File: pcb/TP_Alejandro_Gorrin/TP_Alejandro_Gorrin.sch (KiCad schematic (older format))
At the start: 32 parts, among them J1 Conn_01x12, J2 Conn_01x02, J3 Conn_01x16, J4 USB_B_Micro, Q1 MMBT3904, Q2 MMBT3904, Q3 BS250, SW1 SW_1, U1 MCP73831-2-OT, U3 CP2104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

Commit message: PCB conexiones realizadas
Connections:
- net +3V3: now also J3.1 (Pin_1); no longer J3.15 (Pin_15)
- net A0_DAC2: now also J1.6 (Pin_6); no longer J3.12 (Pin_12)
- net A1_DAC1: now also J1.7 (Pin_7); no longer J3.11 (Pin_11)
- net A2_I34: now also J1.10 (Pin_10); no longer J3.10 (Pin_10)
- net A3_I39: now also J1.11 (Pin_11); no longer J3.9 (Pin_9)
- net A4_IO36: now also J1.12 (Pin_12); no longer J3.8 (Pin_8)
- net A5_IO4: now also J3.8 (Pin_8); no longer J3.7 (Pin_7)
- net EN: now also J3.4 (Pin_4); no longer J1.2 (Pin_2)
- net GNDD: now also J3.3 (Pin_3); no longer J3.13 (Pin_13)
- net IO12_A11: now also J1.3 (Pin_3); no longer J1.5 (Pin_5)
- net IO13_A12: now also J3.6 (Pin_6); no longer J1.4 (Pin_4)
- net IO14_A6: now also J1.4 (Pin_4); no longer J1.10 (Pin_10)
- net IO15_A8: now also J3.7 (Pin_7); no longer J1.8 (Pin_8)
- net IO16: now also J3.9 (Pin_9); no longer J3.3 (Pin_3)
- net IO17: now also J3.10 (Pin_10); no longer J3.2 (Pin_2)
- net IO21: now also J3.14 (Pin_14); no longer J3.1 (Pin_1)
- net IO27_A10: now also J1.5 (Pin_5); no longer J1.6 (Pin_6)
- net IO33_A9: now also J1.8 (Pin_8); no longer J1.7 (Pin_7)
- net MISI: now also J3.12 (Pin_12); no longer J3.5 (Pin_5)
- net MISO: now also J3.13 (Pin_13); no longer J3.4 (Pin_4)
- net RESET: now also J3.2 (Pin_2); no longer J3.16 (Pin_16)
- net SCI: now also J3.15 (Pin_15); no longer J1.11 (Pin_11)
- net SCK: now also J3.11 (Pin_11); no longer J3.6 (Pin_6)
- net SDA: now also J3.16 (Pin_16); no longer J1.12 (Pin_12)
- net VBUS: now also J1.2 (Pin_2); no longer J1.3 (Pin_3)
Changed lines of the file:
@@
 Wire Wire Line
 	3775 6225 3775 6375
-Wire Wire Line
-	3775 5925 3775 5850
 $Comp
 L Transistor_FET:BS250 Q3
@@
 Wire Wire Line
 	6250 4800 5900 4800
-Text Label 5900 4800 0    45   ~ 0
+Text Label 7400 4700 0    45   ~ 0
 IO13_A12
 Text Label 1750 5275 1    47   ~ 0
@@
 $EndComp
 Wire Wire Line
-	6250 4700 5700 4700
-Wire Wire Line
-	5700 4700 5700 4600
+	5700 4600 5700 4500
 Wire Wire Line
 	6250 4500 5900 4500
@@
 L power:VBUS #PWR0122
 U 1 1 5F8AB477
-P 5700 4600
-F 0 "#PWR0122" H 5700 4450 50  0001 C CNN
-F 1 "VBUS" H 5715 4773 50  0000 C CNN
-F 2 "" H 5700 4600 50  0001 C CNN
-F 3 "" H 5700 4600 50  0001 C CNN
-	1    5700 4600
+P 5700 4500
+F 0 "#PWR0122" H 5700 4350 50  0001 C CNN
+F 1 "VBUS" H 5700 4650 50  0000 C CNN
+F 2 "" H 5700 4500 50  0001 C CNN
+F 3 "" H 5700 4500 50  0001 C CNN
+	1    5700 4500
 	1    0    0    -1
 $EndComp
@@
 	1    0    0    -1
 $EndComp
-Wire Wire Line
-	7700 5400 7000 5400
-Wire Wire Line
-	7000 5400 7000 5500
 $Comp
 L power:GNDD #PWR0129
 U 1 1 5F8BAE19
-P 7000 5500
-F 0 "#PWR0129" H 7000 5250 50  0001 C CNN
-F 1 "GNDD" H 7004 5345 50  0000 C CNN
-F 2 "" H 7000 5500 50  0001 C CNN
-F 3 "" H 7000 5500 50  0001 C CNN
-	1    7000 5500
-	1    0    0    -1
-$EndComp
-Wire Wire Line
-	7700 5600 7350 5600
-Wire Wire Line
-	7350 5600 7350 5550
+P 7125 4500
+F 0 "#PWR0129" H 7125 4250 50  0001 C CNN
+F 1 "GNDD" H 7129 4345 50  0000 C CNN
+F 2 "" H 7125 4500 50  0001 C CNN
+F 3 "" H 7125 4500 50  0001 C CNN
+	1    7125 4500
+	1    0    0    -1
+$EndComp
 $Comp
 L power:+3.3V #PWR0130
 U 1 1 5F8BF3BE
-P 7350 5550
-F 0 "#PWR0130" H 7350 5400 50  0001 C CNN
-F 1 "+3.3V" H 7500 5600 50  0000 C CNN
-F 2 "" H 7350 5550 50  0001 C CNN
-F 3 "" H 7350 5550 50  0001 C CNN
-	1    7350 5550
+P 7300 4150
+F 0 "#PWR0130" H 7300 4000 50  0001 C CNN
+F 1 "+3.3V" H 7450 4200 50  0000 C CNN
+F 2 "" H 7300 4150 50  0001 C CNN
+F 3 "" H 7300 4150 50  0001 C CNN
+	1    7300 4150
 	1    0    0    -1
 $EndComp
@@
 	6250 5600 5900 5600
 Wire Wire Line
-	7700 4200 7400 4200
-Wire Wire Line
 	7700 4300 7400 4300
 Wire Wire Line
-	7700 4400 7400 4400
-Wire Wire Line
 	7700 4500 7400 4500
-Wire Wire Line
-	7700 4600 7400 4600
 Wire Wire Line
 	7700 4700 7400 4700
@@
 Text Label 775  3575 0    47   ~ 0
 A3_I39
-Text Label 7400 4900 0    47   ~ 0
+Text Label 5900 5600 0    47   ~ 0
 A4_IO36
-Text Label 7400 5000 0    47   ~ 0
+Text Label 5900 5500 0    47   ~ 0
 A3_I39
 Text Label 3150 3925 0    47   ~ 0
 SCK
-Text Label 7400 4700 0    47   ~ 0
+Text Label 7400 5200 0    47   ~ 0
 SCK
-Wire Wire Line
-	6250 4600 5900 4600
-Text Label 5900 4900 0    47   ~ 0
+Text Label 5900 4700 0    47   ~ 0
 IO12_A11
 Text Label 775  4475 0    47   ~ 0
 IO12_A11
-Text Label 5900 5000 0    47   ~ 0
+Text Label 5900 4900 0    47   ~ 0
 IO27_A10
 Text Label 775  4275 0    47   ~ 0
 IO27_A10
-Text Label 5900 5100 0    47   ~ 0
+Text Label 5900 5200 0    47   ~ 0
 IO33_A9
 Text Label 775  3975 0    47   ~ 0
 IO33_A9
-Text Label 5900 5200 0    47   ~ 0
+Text Label 7400 4800 0    47   ~ 0
 IO15_A8
 Text Label 2450 5275 1    47   ~ 0
@@
 Text Label 775  3875 0    47   ~ 0
 IO32_A7
-Text Label 5900 5400 0    47   ~ 0
+Text Label 5900 4800 0    47   ~ 0
 IO14_A6
 Text Label 775  4375 0    47   ~ 0
 IO14_A6
-Text Label 5900 5500 0    47   ~ 0
+Text Label 7400 5600 0    47   ~ 0
 SCI
 Text Label 3150 3225 0    47   ~ 0
@@
 Text Label 3150 3125 0    47   ~ 0
 SDA
-Text Label 5900 5600 0    47   ~ 0
+Text Label 7400 5700 0    47   ~ 0
 SDA
-Text Label 7400 4200 0    47   ~ 0
+Text Label 7400 5500 0    47   ~ 0
 IO21
 Text Label 3150 3525 0    47   ~ 0
 IO21
-Text Label 7400 4300 0    47   ~ 0
+Text Label 7400 5100 0    47   ~ 0
 IO17
-Text Label 7400 4400 0    47   ~ 0
+Text Label 7400 5000 0    47   ~ 0
 IO16
 Text Label 3150 4025 0    47   ~ 0
@@
 Text Label 3150 4125 0    47   ~ 0
 IO16
-Text Label 7400 4500 0    47   ~ 0
+Text Label 7400 5400 0    47   ~ 0
 MISO
 Text Label 3150 3725 0    47   ~ 0
 MISO
-Text Label 7400 4600 0    47   ~ 0
+Text Label 7400 5300 0    47   ~ 0
 MISI
 Text Label 3150 3825 0    47   ~ 0
 MISI
-Text Label 7400 4800 0    47   ~ 0
+Text Label 7400 4900 0    47   ~ 0
 A5_IO4
 Text Label 3150 4225 0    47   ~ 0
 A5_IO4
-Text Label 7400 5100 0    47   ~ 0
+Text Label 5900 5400 0    47   ~ 0
 A2_I34
 Text Label 775  3675 0    47   ~ 0
 A2_I34
-Text Label 7400 5200 0    47   ~ 0
+Text Label 5900 5100 0    47   ~ 0
 A1_DAC1
 Text Label 775  4075 0    47   ~ 0
 A1_DAC1
-Text Label 7400 5300 0    47   ~ 0
+Text Label 5900 5000 0    47   ~ 0
 A0_DAC2
 Text Label 775  4175 0    47   ~ 0
 A0_DAC2
-Text Label 7400 5700 0    47   ~ 0
+Text Label 7400 4300 0    47   ~ 0
 RESET
 Text Label 4475 3100 0    47   ~ 0
@@
 Text Notes 2225 725  0    55   ~ 11
 POWER_AND_FILTERING
-Text Label 5900 4600 0    47   ~ 0
+Text Label 7400 4500 0    47   ~ 0
 EN
 NoConn ~ 7675 1050
@@
 NoConn ~ 6775 2250
 NoConn ~ 6775 2150
-NoConn ~ 7700 5500
 $Comp
 L Switch:SW_DPST_x2 SW1
@@
 	1875 1325 1750 1325
 Connection ~ 1625 1325
-NoConn ~ 6250 4600
+NoConn ~ 7700 4600
 Wire Wire Line
 	725  725  725  1025
@@
 Wire Wire Line
 	6150 2250 6325 2250
-Wire Wire Line
-	6325 1550 6325 1875
 Wire Wire Line
 	6425 2550 6150 2550
@@
 	1    0    0    -1
 $EndComp
-$Comp
-L power:PWR_FLAG #FLG0103
-U 1 1 5F8B58E7
-P 6225 1875
-F 0 "#FLG0103" H 6225 1950 50  0001 C CNN
-F 1 "PWR_FLAG" V 6225 2025 50  0000 L CNN
-F 2 "" H 6225 1875 50  0001 C CNN
-F 3 "~" H 6225 1875 50  0001 C CNN
-	1    6225 1875
-	0    -1   -1   0
-$EndComp
-Wire Wire Line
-	6225 1875 6325 1875
-Connection ~ 6325 1875
-Wire Wire Line
-	6325 1875 6325 2250
-$Comp
-L power:PWR_FLAG #FLG0105
-U 1 1 5F8C7B1A
-P 3850 5850
-F 0 "#FLG0105" H 3850 5925 50  0001 C CNN
-F 1 "PWR_FLAG" V 3950 5900 50  0000 L CNN
-F 2 "" H 3850 5850 50  0001 C CNN
-F 3 "~" H 3850 5850 50  0001 C CNN
-	1    3850 5850
-	0    1    1    0
-$EndComp
-Wire Wire Line
-	3850 5850 3775 5850
-Connection ~ 3775 5850
-Wire Wire Line
-	3775 5850 3775 5775
 Wire Wire Line
 	3225 1675 3225 2000
@@
 NoConn ~ 2550 4925
 Wire Wire Line
-	5850 2850 5850 3000
-Wire Wire Line
 	4400 1925 4400 1950
 Wire Wire Line
@@
 $EndComp
 NoConn ~ 6150 2650
+Wire Wire Line
+	5700 4600 6250 4600
+Wire Wire Line
+	6250 4700 5900 4700
+Wire Wire Line
+	7300 4200 7300 4150
+Wire Wire Line
+	7300 4200 7700 4200
+Wire Wire Line
+	7700 5400 7400 5400
+Wire Wire Line
+	7700 5500 7400 5500
+Wire Wire Line
+	7700 5600 7400 5600
+Wire Wire Line
+	7125 4400 7125 4500
+Wire Wire Line
+	7125 4400 7700 4400
+NoConn ~ 7700 4500
+Wire Wire Line
+	3775 5775 3775 5925
+Wire Wire Line
+	5850 2850 5850 3000
+Wire Wire Line
+	6325 1550 6325 2250
 $EndSCHEMATC

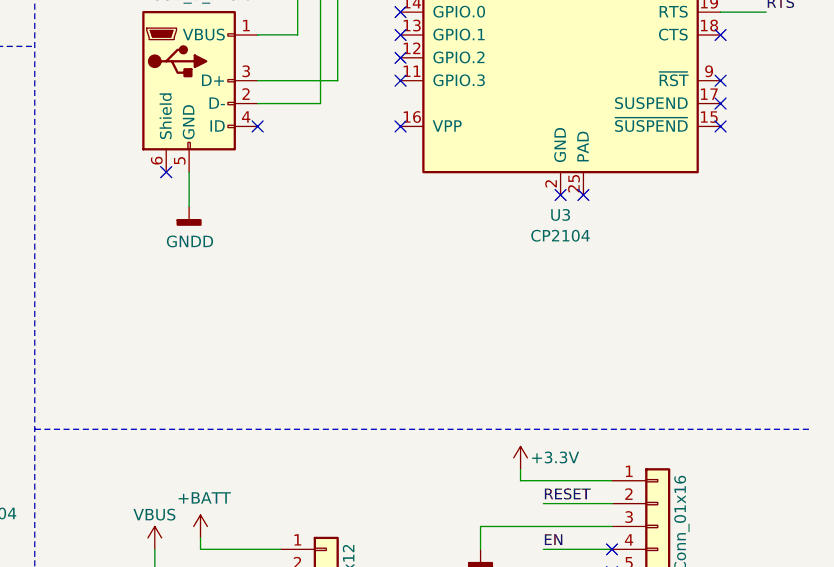
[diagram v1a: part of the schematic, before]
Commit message: Cambio y agrego vias para facilitar el ruteo
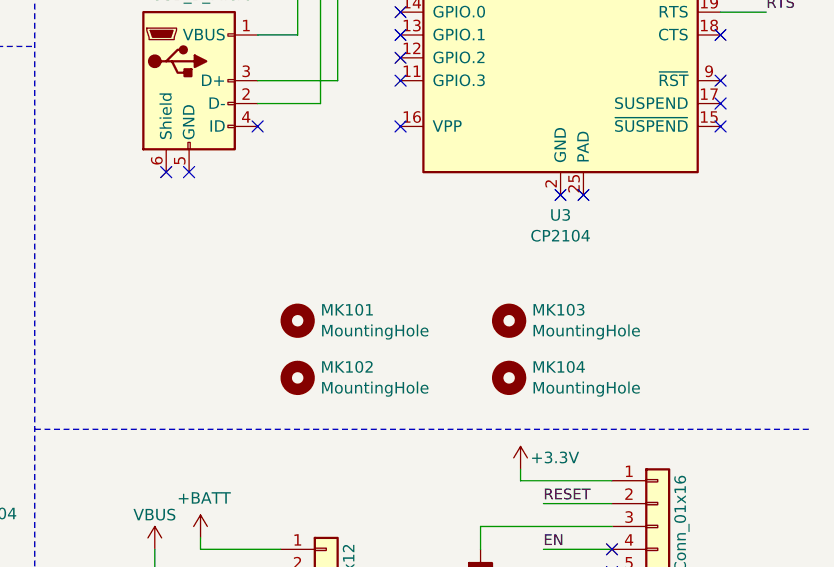
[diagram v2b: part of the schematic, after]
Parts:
- added MK101, MK102, MK103, MK104: MountingHole, MountingHole:MountingHole_2.2mm_M2_DIN965_Pad, symbol Mechanical:MountingHole
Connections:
- net GNDD: no longer J4.5 (GND)
- no-connect marks 28 -> 29
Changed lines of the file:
@@
 Wire Wire Line
 	5925 1200 5925 1250
-$Comp
-L power:GNDD #PWR0112
-U 1 1 5F8A1CC4
-P 5850 3000
-F 0 "#PWR0112" H 5850 2750 50  0001 C CNN
-F 1 "GNDD" H 5854 2845 50  0000 C CNN
-F 2 "" H 5850 3000 50  0001 C CNN
-F 3 "" H 5850 3000 50  0001 C CNN
-	1    5850 3000
-	1    0    0    -1
-$EndComp
 Wire Wire Line
 	5925 1200 6525 1200
@@
 	3775 5775 3775 5925
 Wire Wire Line
-	5850 2850 5850 3000
-Wire Wire Line
 	6325 1550 6325 2250
+NoConn ~ 5850 2850
+$Comp
+L Mechanical:MountingHole MK101
+U 1 1 5FB548C1
+P 6325 3500
+F 0 "MK101" H 6425 3546 50  0000 L CNN
+F 1 "MountingHole" H 6425 3455 50  0000 L CNN
+F 2 "MountingHole:MountingHole_2.2mm_M2_DIN965_Pad" H 6325 3500 50  0001 C CNN
+F 3 "~" H 6325 3500 50  0001 C CNN
+	1    6325 3500
+	1    0    0    -1
+$EndComp
+$Comp
+L Mechanical:MountingHole MK102
+U 1 1 5FB54F64
+P 6325 3750
+F 0 "MK102" H 6425 3796 50  0000 L CNN
+F 1 "MountingHole" H 6425 3705 50  0000 L CNN
+F 2 "MountingHole:MountingHole_2.2mm_M2_DIN965_Pad" H 6325 3750 50  0001 C CNN
+F 3 "~" H 6325 3750 50  0001 C CNN
+	1    6325 3750
+	1    0    0    -1
+$EndComp
+$Comp
+L Mechanical:MountingHole MK103
+U 1 1 5FB55716
+P 7250 3500
+F 0 "MK103" H 7350 3546 50  0000 L CNN
+F 1 "MountingHole" H 7350 3455 50  0000 L CNN
+F 2 "MountingHole:MountingHole_2.2mm_M2_DIN965_Pad" H 7250 3500 50  0001 C CNN
+F 3 "~" H 7250 3500 50  0001 C CNN
+	1    7250 3500
+	1    0    0    -1
+$EndComp
+$Comp
+L Mechanical:MountingHole MK104
+U 1 1 5FB5612A
+P 7250 3750
+F 0 "MK104" H 7350 3796 50  0000 L CNN
+F 1 "MountingHole" H 7350 3705 50  0000 L CNN
+F 2 "MountingHole:MountingHole_2.2mm_M2_DIN965_Pad" H 7250 3750 50  0001 C CNN
+F 3 "~" H 7250 3750 50  0001 C CNN
+	1    7250 3750
+	1    0    0    -1
+$EndComp
 $EndSCHEMATC

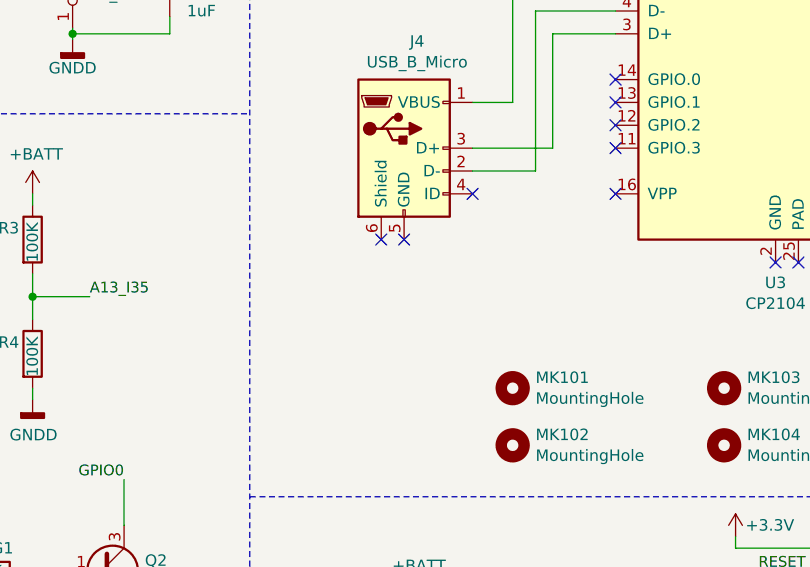
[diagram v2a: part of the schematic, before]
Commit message: Se observa problema con GNDD
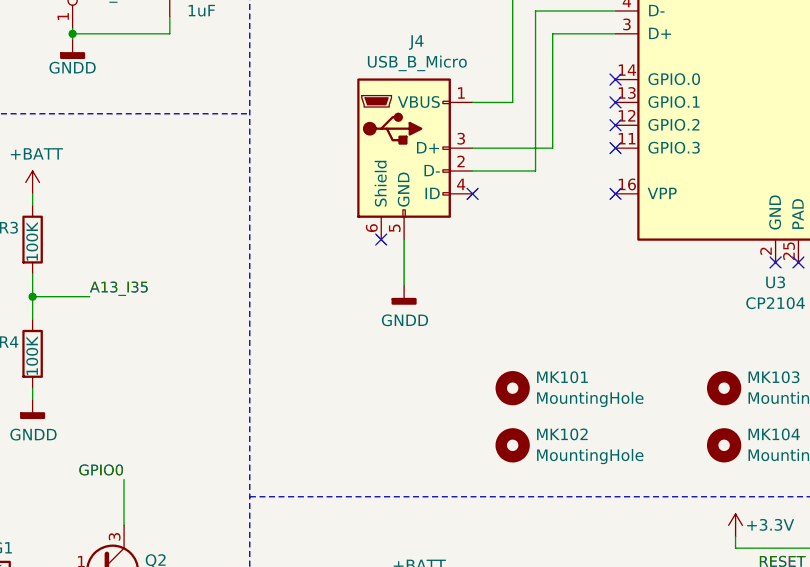
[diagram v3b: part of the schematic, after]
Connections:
- net GNDD: now also J4.5 (GND)
- no-connect marks 29 -> 28
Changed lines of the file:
@@
 Wire Wire Line
 	6325 1550 6325 2250
-NoConn ~ 5850 2850
 $Comp
 L Mechanical:MountingHole MK101
@@
 	1    0    0    -1
 $EndComp
+$Comp
+L power:GNDD #PWR?
+U 1 1 5FB6B73A
+P 5850 3050
+F 0 "#PWR?" H 5850 2800 50  0001 C CNN
+F 1 "GNDD" H 5854 2895 50  0000 C CNN
+F 2 "" H 5850 3050 50  0001 C CNN
+F 3 "" H 5850 3050 50  0001 C CNN
+	1    5850 3050
+	1    0    0    -1
+$EndComp
+Wire Wire Line
+	5850 3050 5850 2850
 $EndSCHEMATC

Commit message: PCB cambios
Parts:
- removed MK103, MK104: MountingHole, MountingHole:MountingHole_2.2mm_M2_DIN965_Pad, symbol Mechanical:MountingHole
- removed Q3: BS250, Package_TO_SOT_THT:TO-92_Inline, symbol Transistor_FET:BS250
- added Q3: DMG3414U, Package_TO_SOT_SMD:SOT-23, symbol Transistor_FET:DMG3414U
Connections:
- net +BATT: now also Q3.2 (S)
- net GNDD: no longer J4.5 (GND)
- net VBUS: now also Q3.1 (G)
- net at C6.1, D4.1 (K), R7.1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: now also Q3.3 (D)
- no-connect marks 28 -> 29
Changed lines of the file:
@@
 	3775 6225 3775 6375
-$Comp
-L Transistor_FET:BS250 Q3
-U 1 1 5F85A103
-P 1275 1025
-F 0 "Q3" H 1479 1071 50  0000 L CNN
-F 1 "BS250" H 1479 980 50  0000 L CNN
-F 2 "Package_TO_SOT_THT:TO-92_Inline" H 1475 950 50  0001 L CIN
-F 3 "http://www.vishay.com/docs/70209/70209.pdf" H 1275 1025 50  0001 L CNN
-	1    1275 1025
-	1    0    0    -1
-$EndComp
 $Comp
 L power:GNDD #PWR0114
@@
 $EndComp
 $Comp
-L Mechanical:MountingHole MK103
-U 1 1 5FB55716
-P 7250 3500
-F 0 "MK103" H 7350 3546 50  0000 L CNN
-F 1 "MountingHole" H 7350 3455 50  0000 L CNN
-F 2 "MountingHole:MountingHole_2.2mm_M2_DIN965_Pad" H 7250 3500 50  0001 C CNN
-F 3 "~" H 7250 3500 50  0001 C CNN
-	1    7250 3500
-	1    0    0    -1
-$EndComp
-$Comp
-L Mechanical:MountingHole MK104
-U 1 1 5FB5612A
-P 7250 3750
-F 0 "MK104" H 7350 3796 50  0000 L CNN
-F 1 "MountingHole" H 7350 3705 50  0000 L CNN
-F 2 "MountingHole:MountingHole_2.2mm_M2_DIN965_Pad" H 7250 3750 50  0001 C CNN
-F 3 "~" H 7250 3750 50  0001 C CNN
-	1    7250 3750
-	1    0    0    -1
-$EndComp
-$Comp
-L power:GNDD #PWR?
-U 1 1 5FB6B73A
-P 5850 3050
-F 0 "#PWR?" H 5850 2800 50  0001 C CNN
-F 1 "GNDD" H 5854 2895 50  0000 C CNN
-F 2 "" H 5850 3050 50  0001 C CNN
-F 3 "" H 5850 3050 50  0001 C CNN
-	1    5850 3050
-	1    0    0    -1
-$EndComp
-Wire Wire Line
-	5850 3050 5850 2850
+L Transistor_FET:DMG3414U Q3
+U 1 1 5FB22527
+P 1275 1025
+F 0 "Q3" H 1479 979 50  0000 L CNN
+F 1 "DMG3414U" H 1479 1070 50  0000 L CNN
+F 2 "Package_TO_SOT_SMD:SOT-23" H 1475 950 50  0001 L CIN
+F 3 "http://www.diodes.com/assets/Datasheets/ds31739.pdf" H 1275 1025 50  0001 L CNN
+	1    1275 1025
+	1    0    0    1
+$EndComp
+NoConn ~ 5850 2850
 $EndSCHEMATC
